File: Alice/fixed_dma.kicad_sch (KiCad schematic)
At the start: 85 parts, among them Q285 NOT_OC, Q286 NOT_OC, Q287 NOT_OC, Q288 NOT_OC, Q289 NOT_OC, Q290 NOT_OC, Q291 NOT_OC, Q292 NOT_OC, Q293 NOT_OC, Q294 NOT_OC, Q295 NOT_OC, Q296 NOT_OC, Q297 NOT_OC, Q298 NOT_OC, Q299 NOT_OC, Q300 NOT_OC, Q301 NOT_OC, Q302 NOT_OC, Q303 NOT_OC, Q304 NOT_OC, Q305 NOT_OC, Q306 NOT_OC, Q307 NOT_OC, Q308 NOT_OC, Q309 NOT_OC, Q310 NOT_OC, Q311 NOT_OC, Q312 NOT_OC, Q313 NOT_OC, Q314 NOT_OC, Q315 NOT_OC, Q316 NOT_OC, Q317 NOT_OC, Q318 NOT_OC, Q319 NOT_OC, Q320 NOT_OC, Q321 NOT_OC

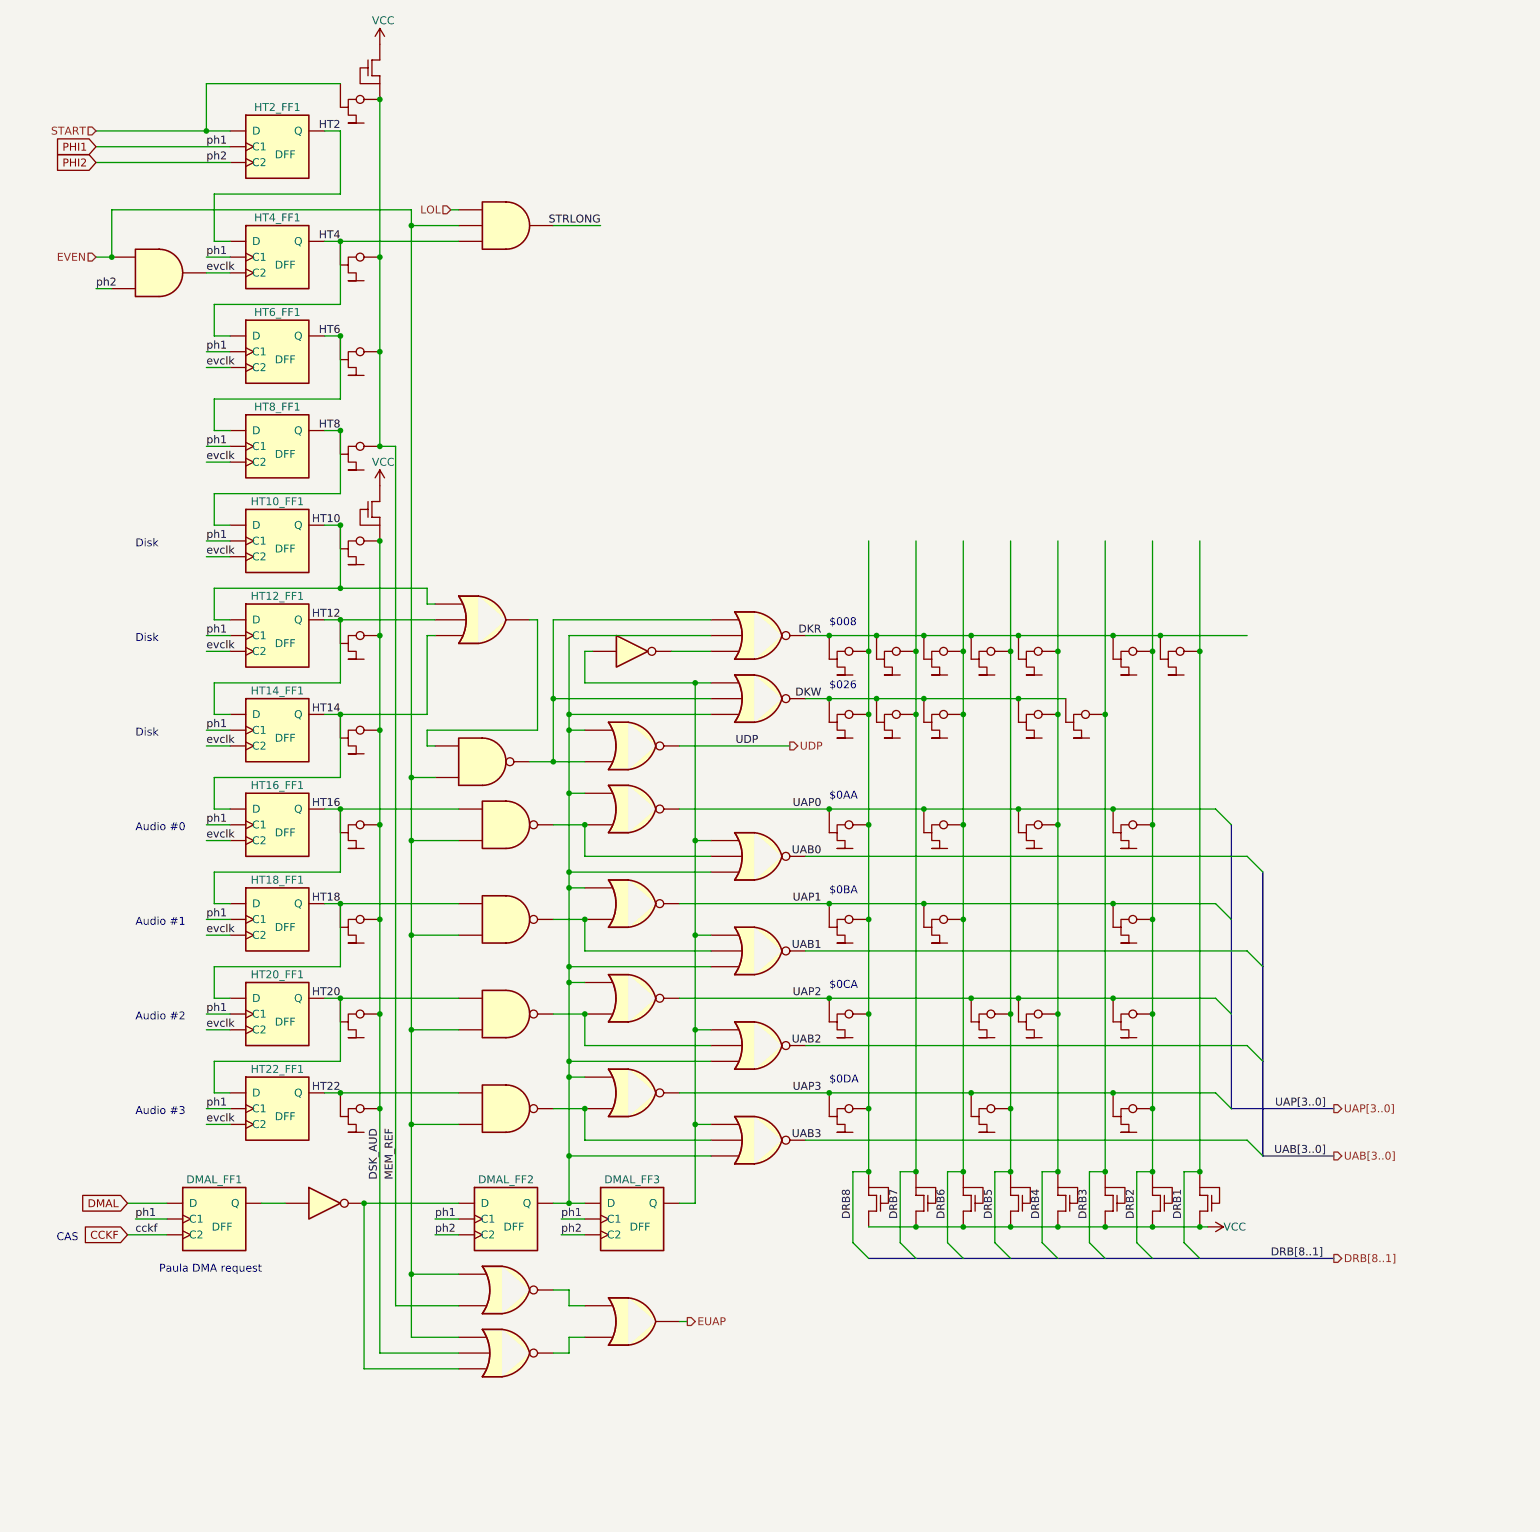
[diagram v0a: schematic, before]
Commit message: Fixed DMA sheet updated
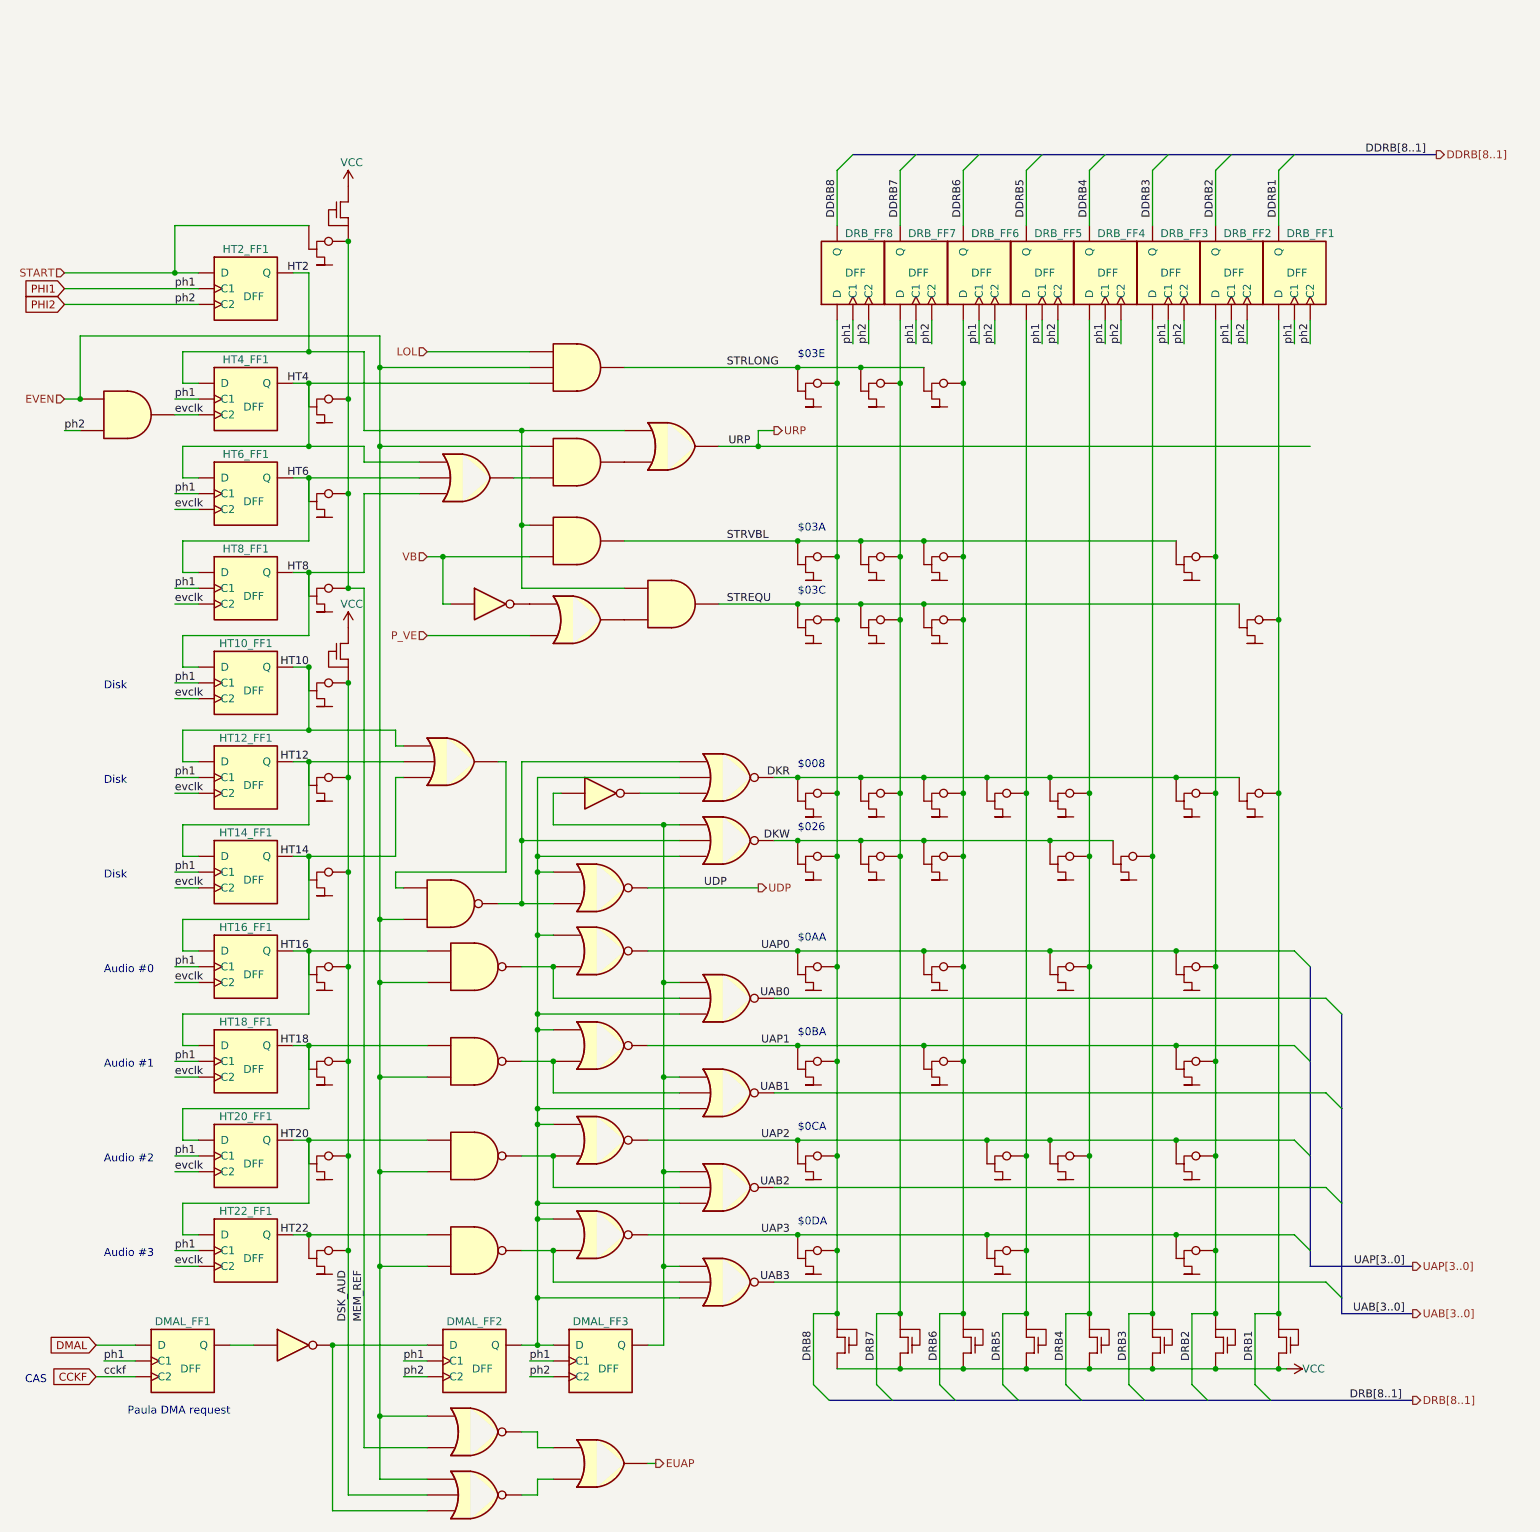
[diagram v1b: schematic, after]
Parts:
- added AND_44, AND_45, AND_46: AND2, symbol NMOS:AND2
- added DRB_FF1, DRB_FF2, DRB_FF3, DRB_FF4, DRB_FF5, DRB_FF6, DRB_FF7, DRB_FF8: DFF, symbol NMOS:DFF
- added NOT_18: NOT, symbol NMOS:NOT
- added OR_24: OR3, symbol NMOS:OR3
- added OR_25, OR_26: OR2, symbol NMOS:OR2
- added Q322, Q323, Q324, Q325, Q326, Q327, Q328, Q329, Q330, Q331, Q332: NOT_OC, symbol NMOS:NOT_OC
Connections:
- net DRB1: now also DRB_FF1.3 (D), Q332.1
- net DRB2: now also DRB_FF2.3 (D), Q331.1
- net DRB3: now also DRB_FF3.3 (D)
- net DRB4: now also DRB_FF4.3 (D)
- net DRB5: now also DRB_FF5.3 (D)
- net DRB6: now also DRB_FF6.3 (D), Q328.1, Q329.1, Q330.1
- net DRB7: now also DRB_FF7.3 (D), Q325.1, Q326.1, Q327.1
- net DRB8: now also DRB_FF8.3 (D), Q322.1, Q323.1, Q324.1
- net EVEN: now also AND_44.2
- net HT2: now also AND_45.2, AND_46.2, OR_26.2
- net HT4: now also OR_24.2
- net HT6: now also OR_24.3
- net HT8: now also OR_24.4
- net PHI1: now also DRB_FF1.4 (C1), DRB_FF2.4 (C1), DRB_FF3.4 (C1), DRB_FF4.4 (C1), DRB_FF5.4 (C1), DRB_FF6.4 (C1), DRB_FF7.4 (C1), DRB_FF8.4 (C1)
- net PHI2: now also DRB_FF1.5 (C2), DRB_FF2.5 (C2), DRB_FF3.5 (C2), DRB_FF4.5 (C2), DRB_FF5.5 (C2), DRB_FF6.5 (C2), DRB_FF7.5 (C2), DRB_FF8.5 (C2)
- net STRLONG: now also Q322.2, Q325.2, Q328.2
- new net: AND_44.3, OR_24.1
- new net: AND_44.1, OR_26.3
- new net: NOT_18.1, OR_25.2
- new net: AND_46.3, OR_25.1
- new net DDRB1: DRB_FF1.1 (Q)
- new net DDRB2: DRB_FF2.1 (Q)
- new net DDRB3: DRB_FF3.1 (Q)
- new net DDRB4: DRB_FF4.1 (Q)
- new net DDRB5: DRB_FF5.1 (Q)
- new net DDRB6: DRB_FF6.1 (Q)
- new net DDRB7: DRB_FF7.1 (Q)
- new net DDRB8: DRB_FF8.1 (Q)
- new net P_VE: OR_25.3
- new net STREQU: AND_46.1, Q324.2, Q327.2, Q330.2, Q332.2
- new net STRVBL: AND_45.1, Q323.2, Q326.2, Q329.2, Q331.2
- new net URP: OR_26.1
- new net VB: AND_45.3, NOT_18.2
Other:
- note added: "$03A"
- note added: "$03C"
- note added: "$03E"
- moved on the sheet: DMAL_FF1, DMAL_FF2, DMAL_FF3, HT10_FF1, HT12_FF1, HT14_FF1, HT16_FF1, HT18_FF1, HT20_FF1, HT22_FF1, HT2_FF1, HT4_FF1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

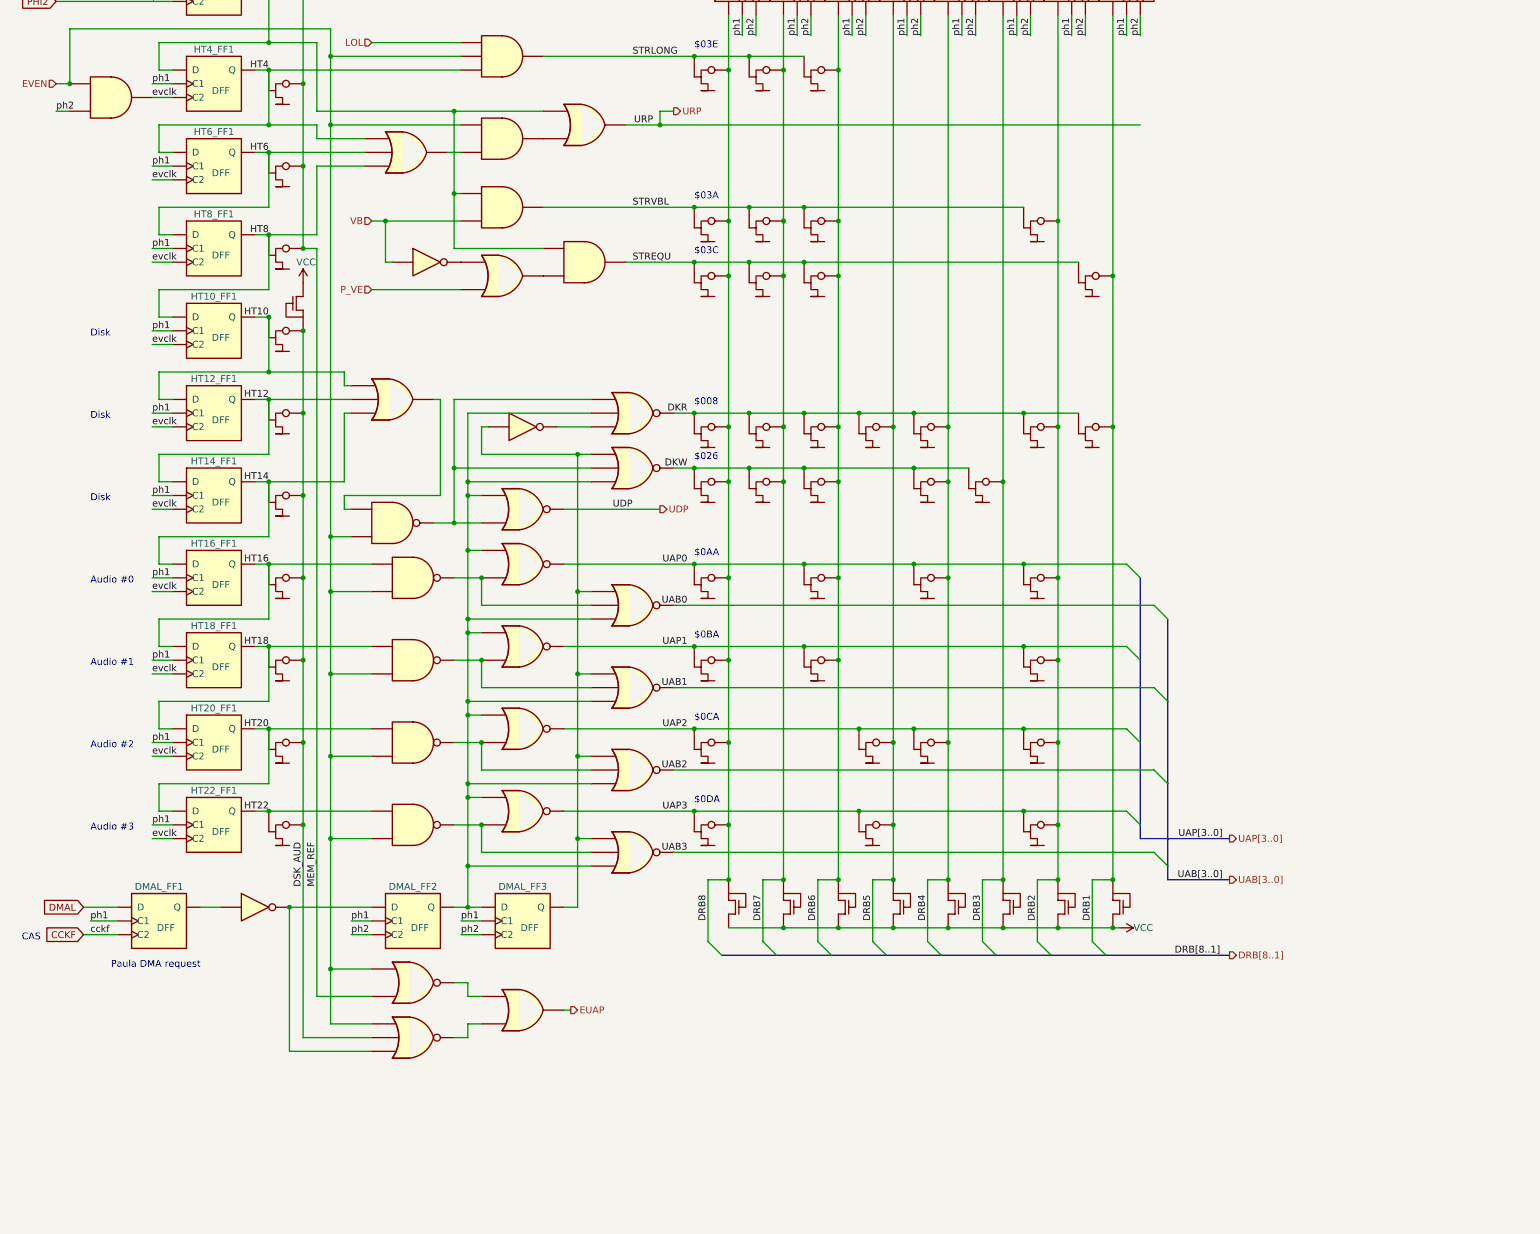
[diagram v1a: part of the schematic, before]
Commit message: Fixed CAS clock polarity, added DMA priority logic
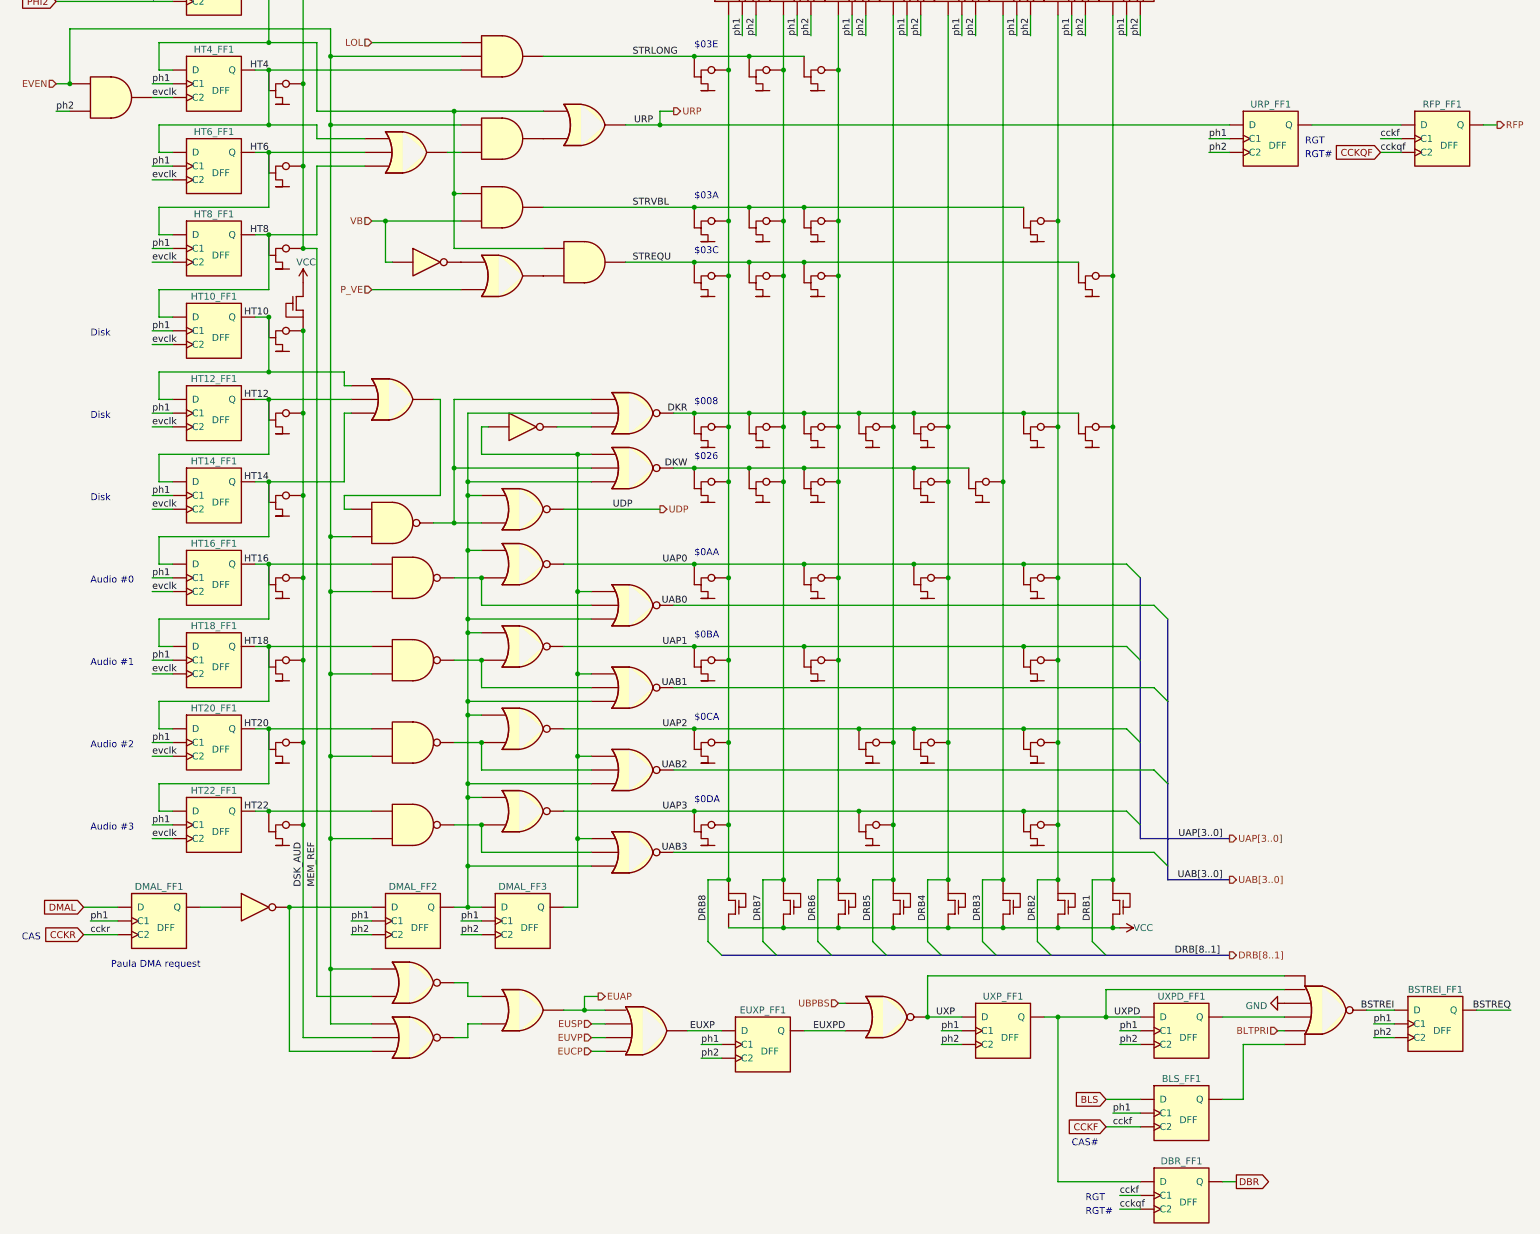
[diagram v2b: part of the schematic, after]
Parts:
- added BLS_FF1, BSTREI_FF1, DBR_FF1, EUXP_FF1, RFP_FF1, URP_FF1, UXPD_FF1, UXP_FF1: DFF, symbol NMOS:DFF
- added NOR_19: NOR2, symbol NMOS:NOR2
- added NOR_20: NOR6, symbol NMOS:NOR6
- added OR_27: OR4, symbol NMOS:OR4
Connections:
- net CCKF: now also BLS_FF1.5 (C2), DBR_FF1.4 (C1), RFP_FF1.4 (C1); no longer DMAL_FF1.5 (C2)
- net EUAP: now also OR_27.2
- net PHI1: now also BLS_FF1.4 (C1), BSTREI_FF1.4 (C1), EUXP_FF1.4 (C1), URP_FF1.4 (C1), UXPD_FF1.4 (C1), UXP_FF1.4 (C1)
- net PHI2: now also BSTREI_FF1.5 (C2), EUXP_FF1.5 (C2), URP_FF1.5 (C2), UXPD_FF1.5 (C2), UXP_FF1.5 (C2)
- net URP: now also URP_FF1.3 (D)
- new net: RFP_FF1.3 (D), URP_FF1.1 (Q)
- new net: NOR_20.5, UXPD_FF1.1 (Q)
- new net: BLS_FF1.1 (Q), NOR_20.7
- new net BLS: BLS_FF1.3 (D)
- new net BLTPRI: NOR_20.6
- new net BSTREI: BSTREI_FF1.3 (D), NOR_20.1
- new net BSTREQ: BSTREI_FF1.1 (Q)
- new net CCKQF: DBR_FF1.5 (C2), RFP_FF1.5 (C2)
- new net CCKR: DMAL_FF1.5 (C2)
- new net DBR: DBR_FF1.1 (Q)
- new net EUCP: OR_27.5
- new net EUSP: OR_27.3
- new net EUVP: OR_27.4
- new net EUXP: EUXP_FF1.3 (D), OR_27.1
- new net EUXPD: EUXP_FF1.1 (Q), NOR_19.3
- new net GND: NOR_20.4
- new net RFP: RFP_FF1.1 (Q)
- new net UBPBS: NOR_19.2
- new net UXP: NOR_19.1, NOR_20.2, UXP_FF1.3 (D)
- new net UXPD: DBR_FF1.3 (D), NOR_20.3, UXPD_FF1.3 (D), UXP_FF1.1 (Q)
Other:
- note added: "CAS#"
- note added: "RGT"
- note added: "RGT#"
